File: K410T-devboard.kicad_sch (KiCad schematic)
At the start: 0 parts

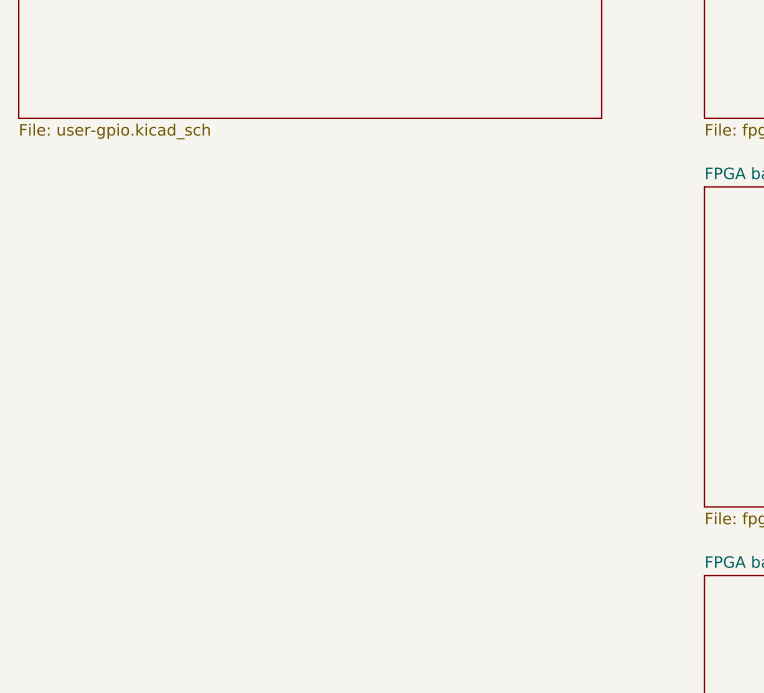
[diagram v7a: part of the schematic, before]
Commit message: Add USB host controller with SPI interface
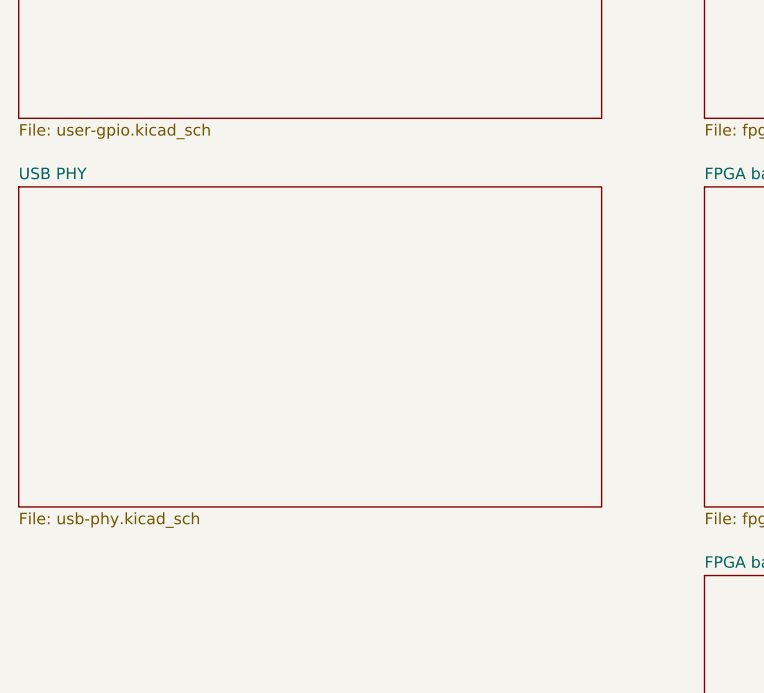
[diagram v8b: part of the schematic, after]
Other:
- added sheet USB PHY (usb-phy.kicad_sch)
